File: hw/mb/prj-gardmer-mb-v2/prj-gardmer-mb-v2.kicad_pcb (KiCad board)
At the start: 2 copper layers, 147 x 71 mm, 176 parts, among them J1 Conn_01x05, J2 230VAC_IN, J3 Conn_01x04, J4 5VDC_IN, K1 AZ9371T-1A-5D, K2 AZ9371T-1A-5D, K3 AZ9371T-1A-5D, K4 AZ9371T-1A-5D, Q1 BC817, Q13 BC817, Q14 BC817, Q2 BC817, Q3 BC817, Q4 BC817, Q5 BC807, Q6 BC807, Q7 BC807, Q8 BC807, Q9 BC817, SW1 Reset_SW, SW10 Unlock_SW, SW2 Clear_SW, SW3 Minutes_SW, SW4 Hours_SW, SW5 Mode_SW, SW6 Relay1_SW, SW7 Relay2_SW, SW8 Relay3_SW, SW9 Relay4_SW, U1 PIC18F25Q10, U2 PCF8523T, U3 74LS166, U4 74HC595, U5 74HC595, U6 ULN2803A, U7 KW4-804AVB, U8 74HC595, Y1 8MHz, Y2 32.768kHz

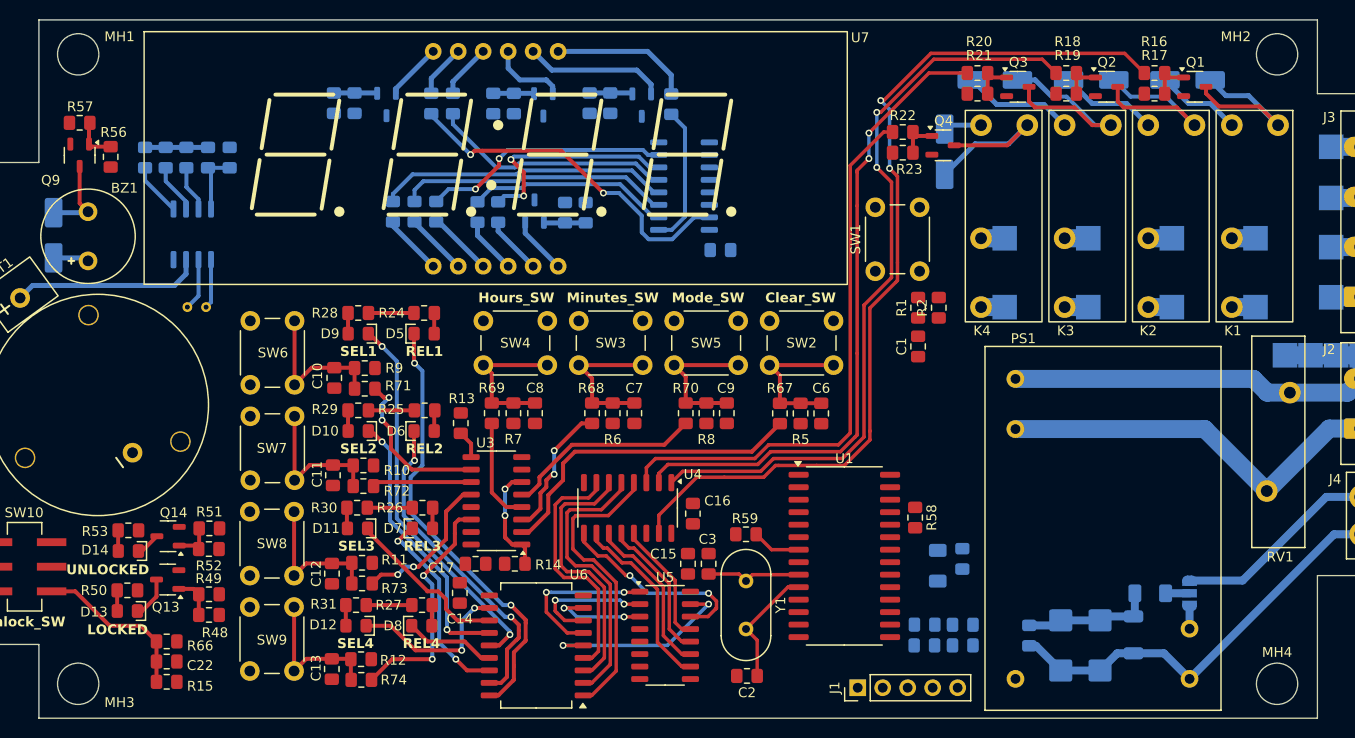
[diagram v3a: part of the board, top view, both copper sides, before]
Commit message: Updated schematic (footprints assign), PCB and footprints: - Changed the 'Generic' footprints that were used for capacitors, resistors and fuses into specific ones (I.e. Generic_0805 is replaced by C_0805 and R_0805). - Differentiated the D_0805 and LED_0805 footprints
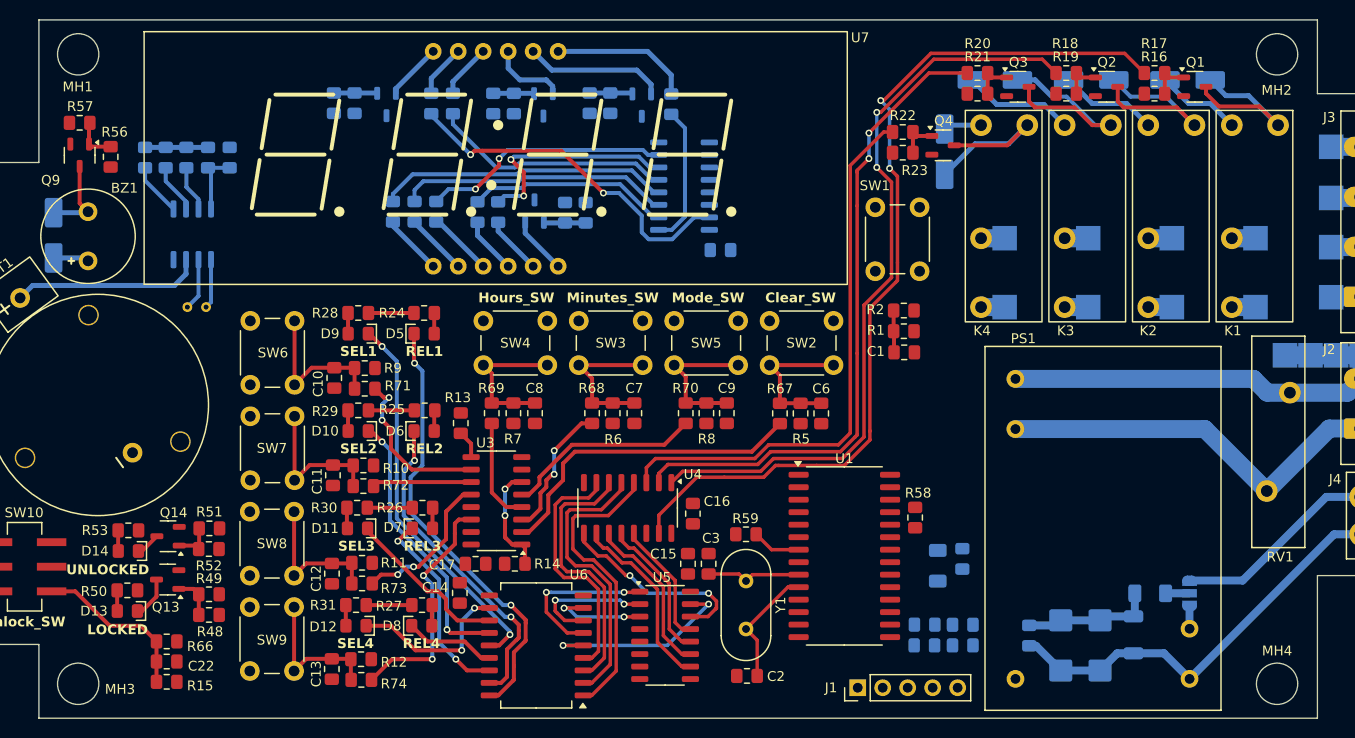
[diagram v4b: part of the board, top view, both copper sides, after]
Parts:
- C1, C10, C11, C12, C13, C14, C15, C16, C17, C19, C2, C21, C22, C3, C4, C5, C6, C7, C8, C9: footprint alf64:Generic_0805 -> alf64:C_0805
- D10, D11, D12, D13, D14, D5, D6, D7, D8, D9: footprint alf64:D_0805 -> alf64:LED_0805
- F1: footprint alf64:Generic_1206 -> alf64:Fuse_1206
- R1, R10, R11, R12, R13, R14, R15, R16, R17, R18, R19, R2, R20, R21, R22, R23, R24, R25, R26, R27, R28, R29, R3, R30, R31, R32, R33, R34, R35, R36, R37, R38, R39, R4, R40, R41, R42, R43, R44, R45, R46, R47, R48, R49, R5, R50, R51, R52, R53, R54, R55, R56, R57, R58, R59, R6, R60, R61, R62, R63, R66, R67, R68, R69, R7, R70, R71, R72, R73, R74, R8, R9: footprint alf64:Generic_0805 -> alf64:R_0805
- moved R2 3.56 mm to (171.4, 84.8), turned to 180 degrees
- moved R1 2.79 mm to (171.4, 87.0), turned to 180 degrees
- moved C1 1.53 mm to (171.5, 89.1), turned to 0 degrees
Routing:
- net Net-(C1-Pad1): track 0.00 -> 4.27 mm

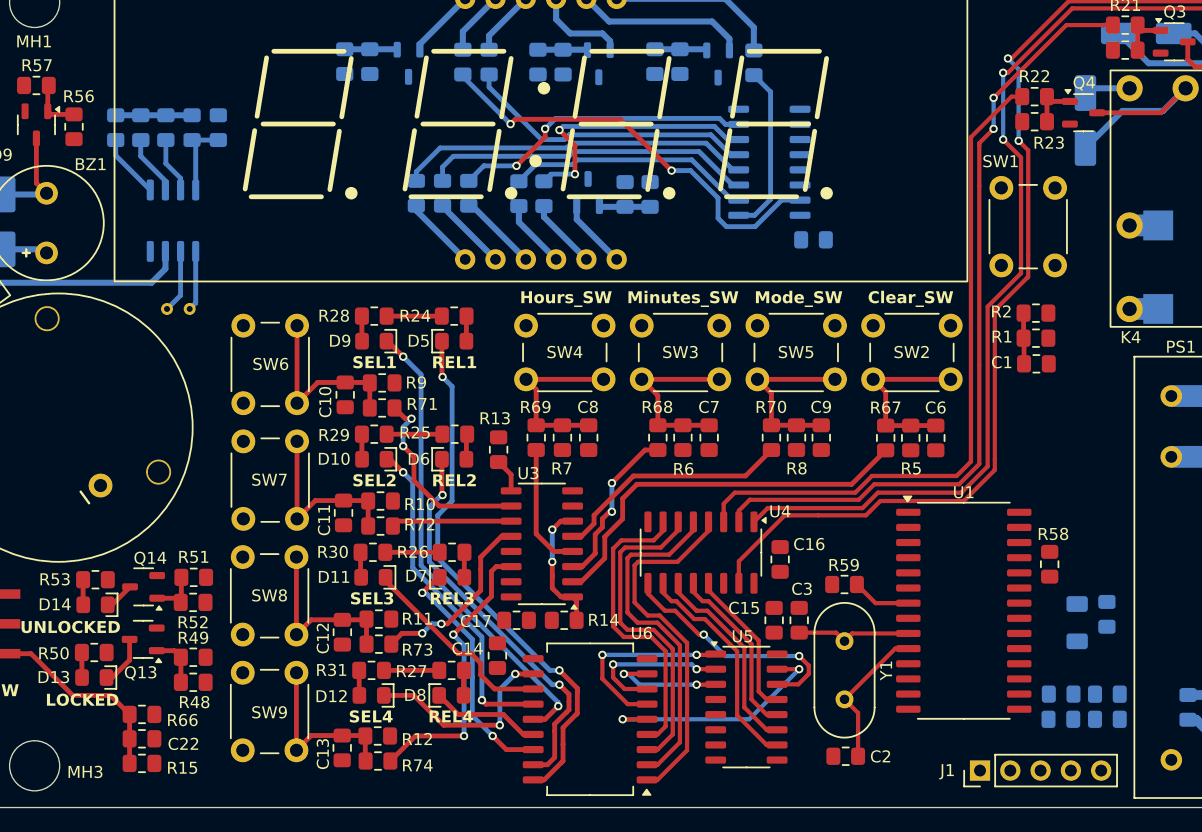
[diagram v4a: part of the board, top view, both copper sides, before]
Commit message: Updated PCB:  - signal traces routed
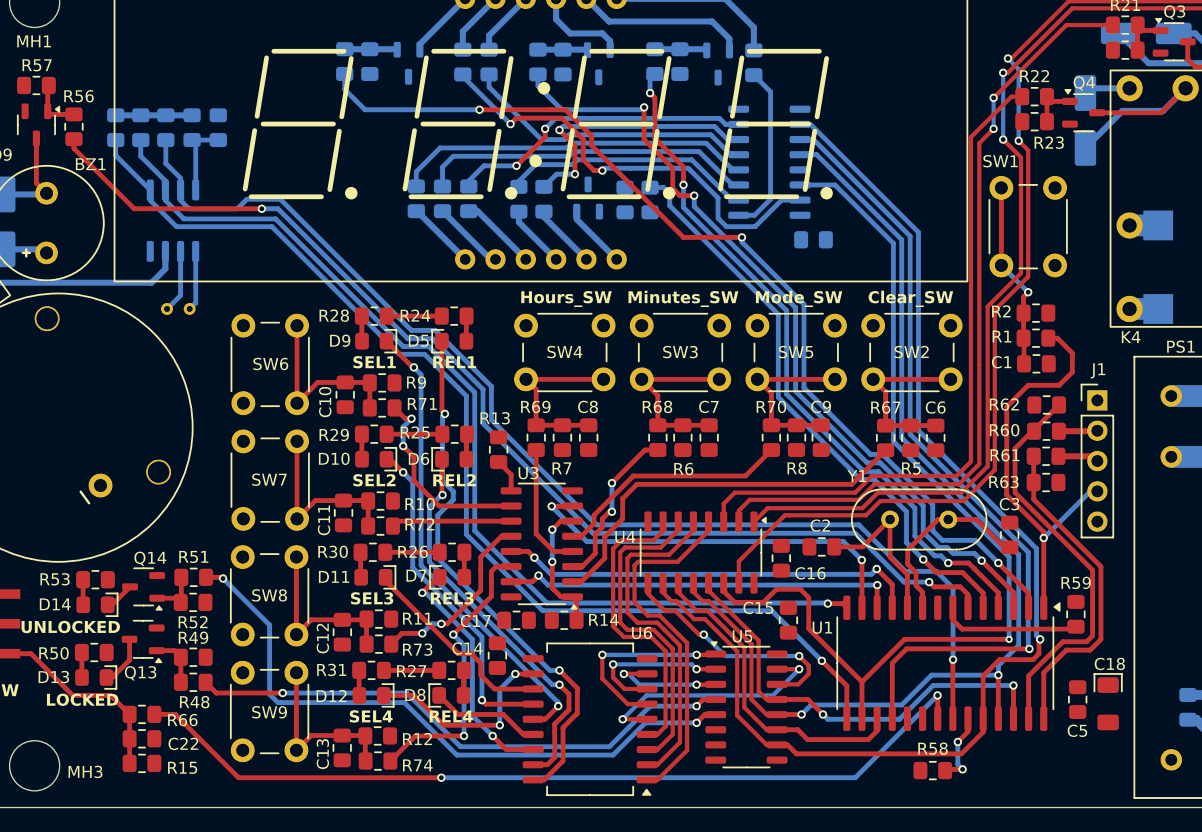
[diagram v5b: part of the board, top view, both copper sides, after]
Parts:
- C18, C5, R60, R61, R62, R63: moved to F.Cu
- moved J1 26.4 mm to (176.6, 97.2), turned to 0 degrees
- moved R62 24.8 mm to (172.3, 92.5)
- moved R60 24.7 mm to (172.3, 94.8)
- moved R61 20.0 mm to (172.3, 96.8), turned to 0 degrees
- moved R63 19.9 mm to (172.3, 99.0)
- moved R58 19.9 mm to (162.8, 123.2), turned to 180 degrees
- moved R59 19.6 mm to (174.8, 110.1), turned to 90 degrees
- moved C3 19.0 mm to (169.2, 103.5)
- moved C2 17.7 mm to (153.5, 104.5)
- moved Y1 14.1 mm to (161.7, 102.2), turned to 180 degrees
- moved C5 7.56 mm to (174.9, 117.2)
- moved C18 7.28 mm to (177.5, 117.6)
- moved U1 4.67 mm to (163.8, 114.2), turned to -90 degrees
- moved C15 1.20 mm to (150.7, 110.6)
- moved Q8 0.46 mm to (133.9, 75.2)
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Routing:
- net Net-(U1-RA4): track 0.00 -> 94.0 mm, vias 0 -> 2
- net Net-(U1-INT1/RB1): track 4.70 -> 97.1 mm, vias 0 -> 1
- net Net-(U1-RC4/SDA1): track 5.39 -> 91.1 mm, vias 0 -> 1
- net /Display/DISP_CA1: track 0.00 -> 83.4 mm, vias 0 -> 3
- net /RelaysLeds/S_SRCLR: track 18.8 -> 100.6 mm, vias 0 -> 1
- net /RelaysLeds/S_SER: track 0.00 -> 81.8 mm, vias 0 -> 1
- net Net-(U1-RC3/SCL1): track 5.04 -> 84.0 mm, vias 0 -> 1
- net /RelaysLeds/S_RCLK: track 14.7 -> 91.0 mm, vias 0 -> 2
- net Net-(U1-INT0/RB0): track 0.00 -> 72.7 mm, vias 0 -> 2
- net /Display/DISP_CA2: track 0.00 -> 68.4 mm, vias 0 -> 3
- net /Display/S_SRCLK2_IN: track 0.00 -> 68.0 mm, vias 0 -> 1
- net /Display/DISP_CA3: track 0.00 -> 59.0 mm, vias 0 -> 3
- net /RelaysLeds/UNLOCK_LED_EN: track 0.00 -> 53.7 mm, vias 0 -> 2
- net /Display/DISP_CA4: track 0.00 -> 49.4 mm, vias 0 -> 1
- net /RelaysLeds/LOCK_LED_EN: track 0.00 -> 46.6 mm, vias 0 -> 2
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
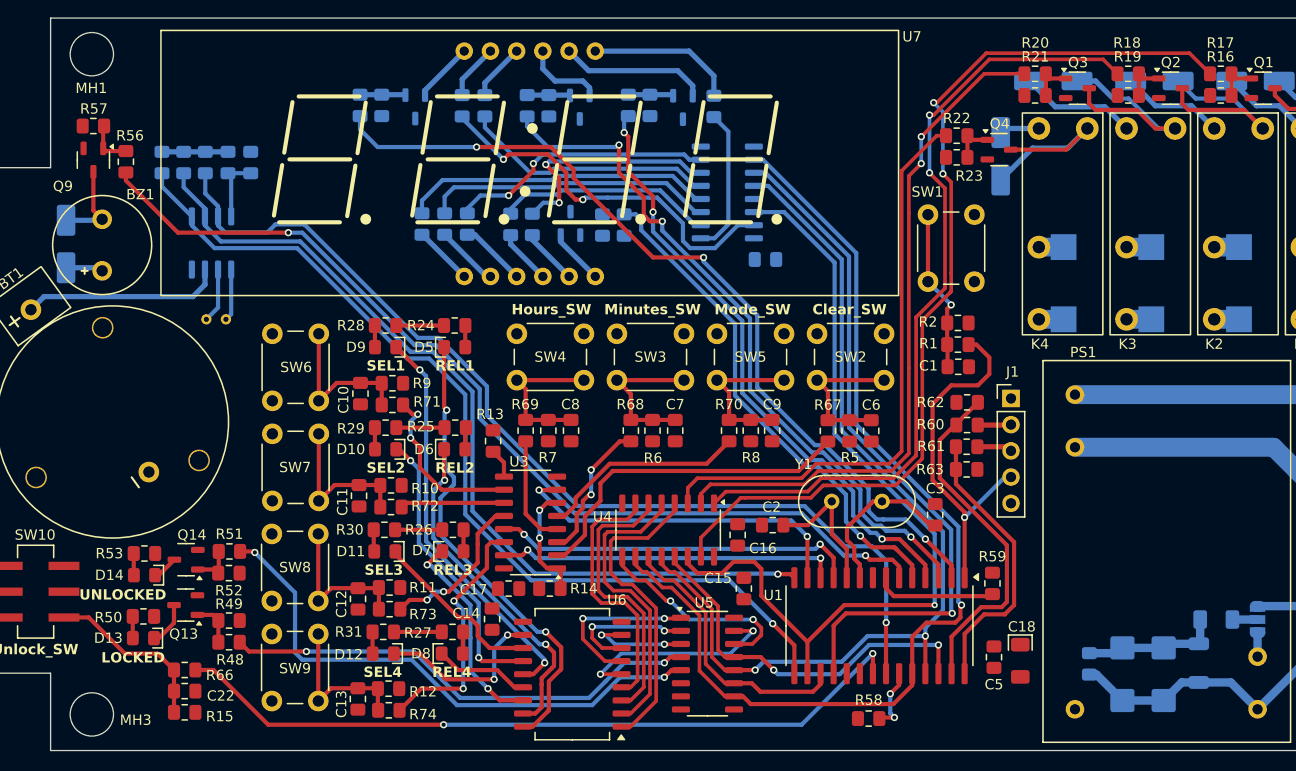
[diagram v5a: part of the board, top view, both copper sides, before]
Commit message: Updated PCB:  - 5V line routed
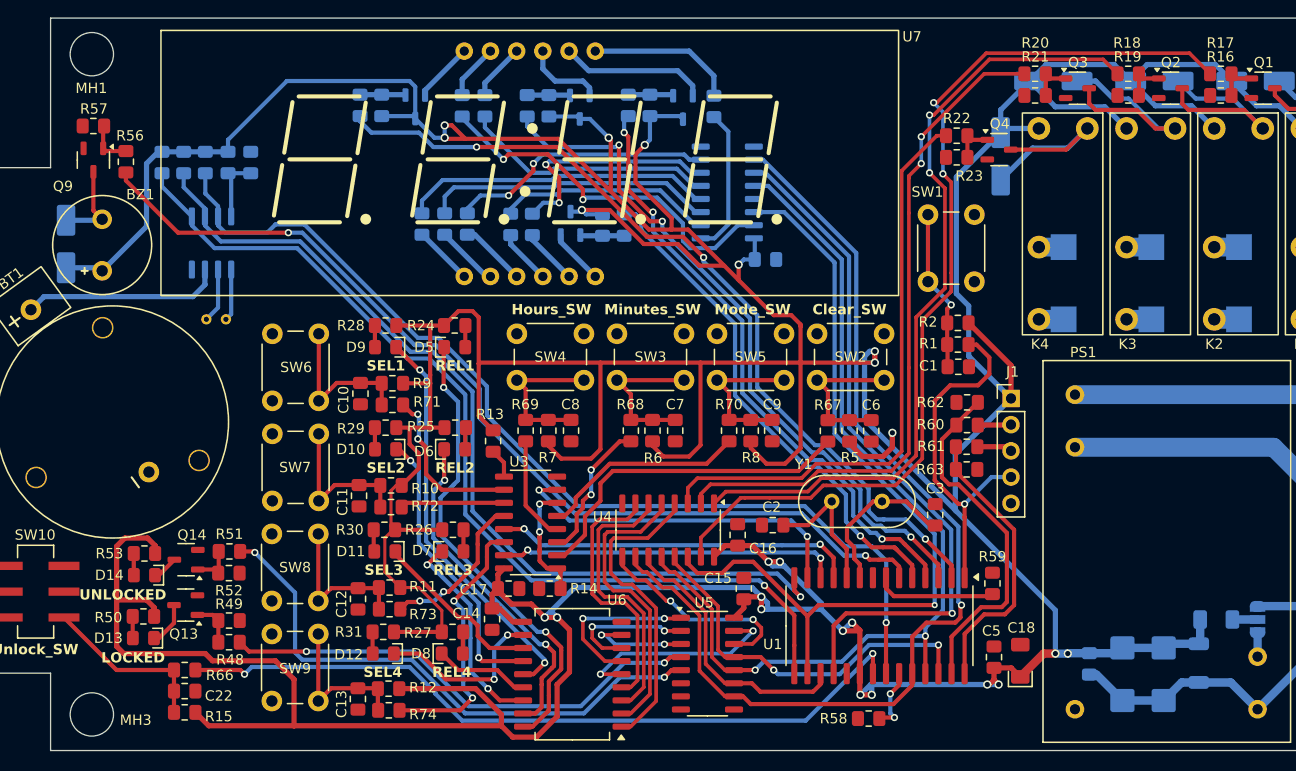
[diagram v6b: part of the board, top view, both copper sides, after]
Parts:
- turned C18 to 90 degrees
- turned C5 to 90 degrees
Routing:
- net +5V: track 76.6 -> 700.3 mm, vias 0 -> 23
- net Net-(Q8-B): track 0.00 -> 4.28 mm
- net Net-(U1-RC3/SCL1): track 84.0 -> 87.5 mm
- net Net-(U3-H): track 24.4 -> 26.2 mm
- net Net-(U1-RC4/SDA1): track 91.1 -> 92.8 mm
- net /RelaysLeds/S_SER: track 81.8 -> 80.7 mm
- net /Display/DISP_CA1: track 83.4 -> 82.5 mm
- net /RelaysLeds/LOCK_LED_EN: track 46.6 -> 47.3 mm
- net /RelaysLeds/UNLOCK_LED_EN: track 53.7 -> 54.4 mm

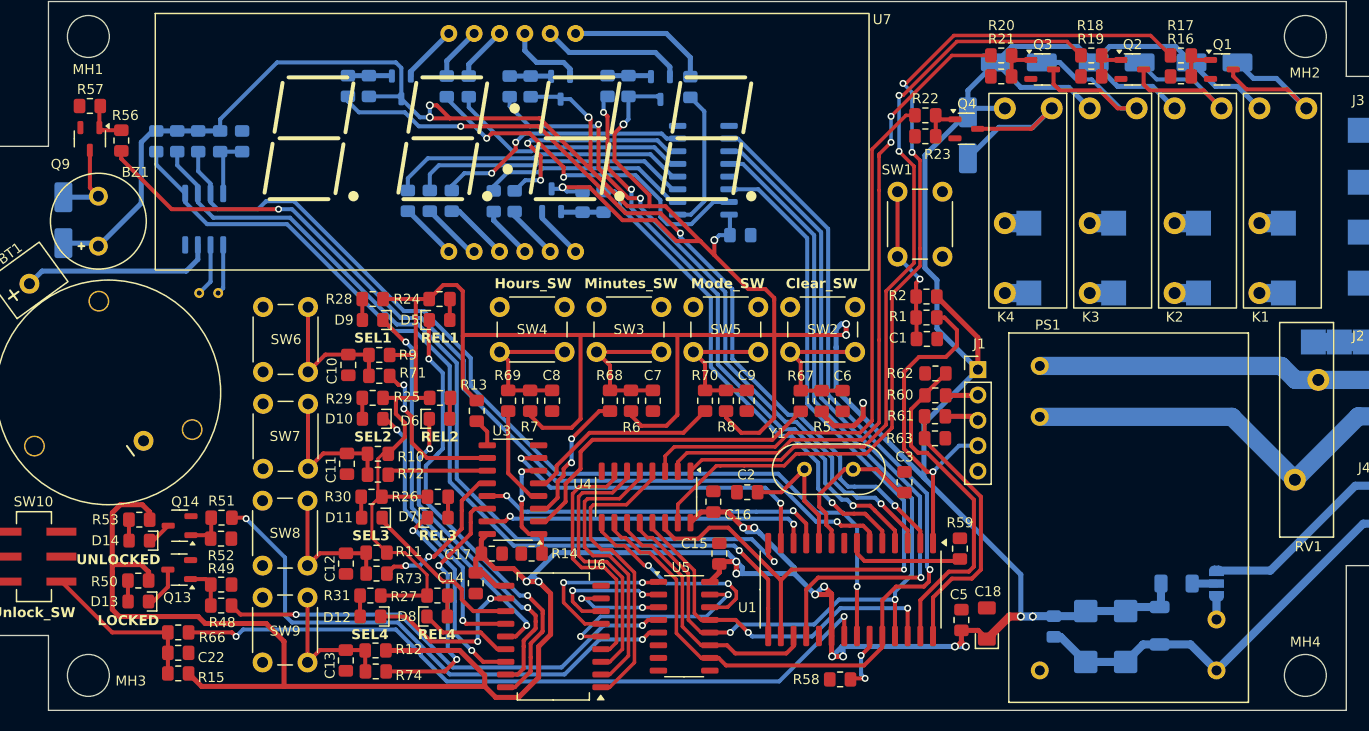
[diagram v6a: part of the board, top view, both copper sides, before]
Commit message: Updated PCB: - GND line routed
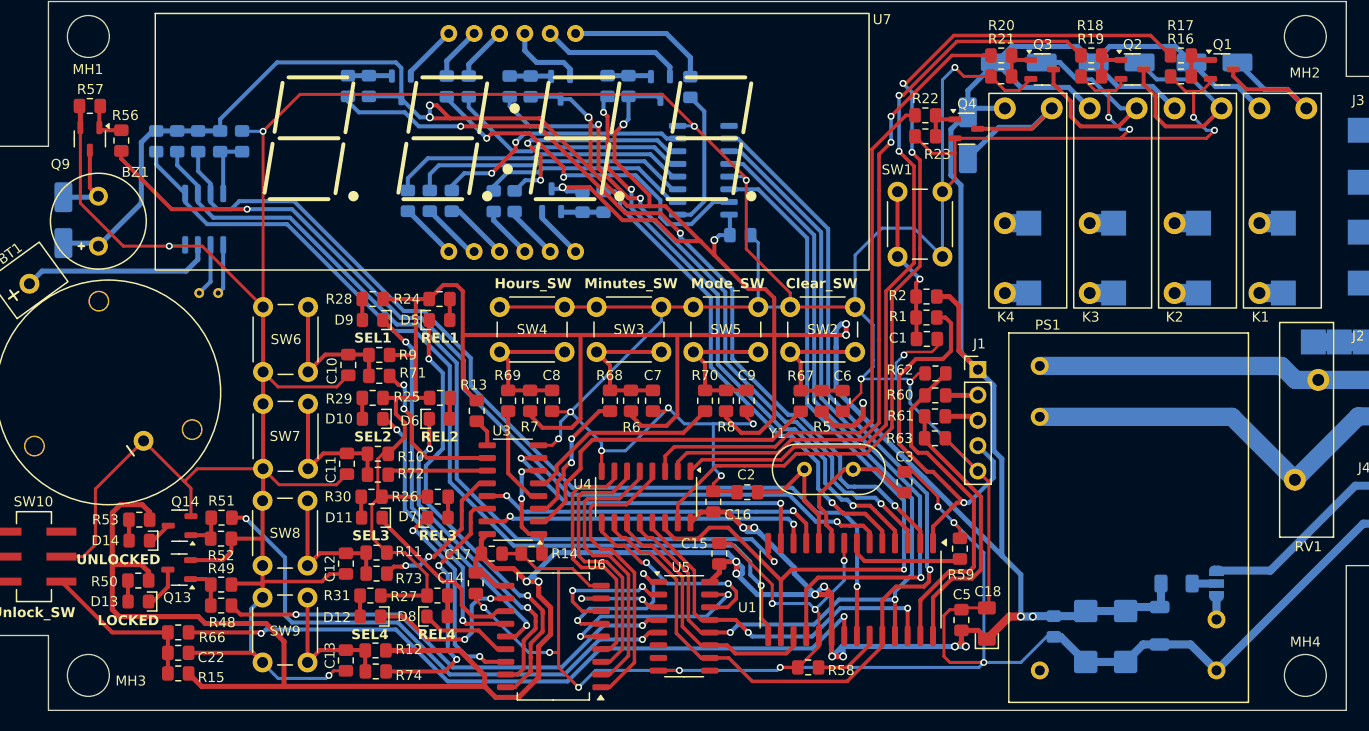
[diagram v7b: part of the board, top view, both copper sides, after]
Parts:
- moved R58 3.42 mm to (159.6, 122.0)
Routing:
- net GND: track 42.7 -> 714.5 mm, vias 0 -> 30
- net +5V: track 700.3 -> 709.0 mm
- net /MCU/MCLR: track 34.8 -> 40.1 mm
- net Net-(D2-A): track 20.4 -> 23.1 mm
- net Net-(D3-A): track 22.2 -> 24.6 mm
- net /RelaysLeds/S_SRCLR: track 100.6 -> 101.9 mm
- net Net-(D11-K): track 17.0 -> 17.8 mm
- net Net-(U1-INT2/RB2): track 6.27 -> 6.95 mm, vias 2 -> 0
- net Net-(D7-K): track 20.7 -> 21.3 mm
